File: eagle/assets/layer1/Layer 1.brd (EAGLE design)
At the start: 196 x 185.9 mm, 246 parts, among them M1C1 33nF, M1C2 680uF, M1C3 1.0uF, M1D1 RED, M1D2 BLUE, M1J1 XT30PB-F, M1Q1 AOD482, M1R1 1k, M1R10 1k, M1R11 10k, M1R12 4.7k, M1R2 1k, M1R3 3.3k, M1R4 3.3k, M1R5 1k, M1R6 1k, M1R7 1k, M1R8 10k, M1R9 10k, M2C1 33nF, M2C2 680uF, M2C3 1.0uF, M2D1 RED, M2D2 BLUE, M2J1 XT30PB-F, M2Q1 AOD482, M2R1 1k, M2R10 1k, M2R11 10k, M2R12 4.7k, M2R2 1k, M2R3 3.3k, M2R4 3.3k, M2R5 1k, M2R6 1k, M2R7 1k, M2R8 10k, M2R9 10k, M3C1 33nF, M3C2 680uF, M3C3 1.0uF, M3D1 RED, M3D2 BLUE, M3J1 XT30PB-F, M3Q1 AOD482, M3R1 1k, M3R10 1k, M3R11 10k, M3R12 4.7k, M3R2 1k, M3R3 3.3k, M3R4 3.3k, M3R5 1k, M3R6 1k, M3R7 1k, M3R8 10k, M3R9 10k, M4C1 33nF, M4C2 680uF, M4C3 1.0uF, M4D1 RED, M4D2 BLUE, M4J1 XT30PB-F, M4Q1 AOD482, M4R1 1k, M4R10 1k, M4R11 10k, M4R12 4.7k, M4R2 1k, M4R3 3.3k, M4R4 3.3k, M4R5 1k, M4R6 1k, M4R7 1k, M4R8 10k, M4R9 10k, Q37 AO3402, X2 SM06B-SRSS-TB, Y1 8MHz

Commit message: -
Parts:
- moved V_BATT_M4B 262.8 mm to (32.5, -82.0)
- moved GND_M2B 260.6 mm to (34.0, -59.5)
- moved GND_M4B 259.5 mm to (34.0, -62.0)
- moved V_BATT_M3B 251.3 mm to (32.5, -79.5)
- moved V_BATT_M2B 239.9 mm to (32.5, -77.0)
- moved V_BATT_M1B 228.7 mm to (32.5, -74.5)
- moved M3J1 47.8 mm to (-3.00, -39.5)
- moved M3D2 45.1 mm to (-7.00, -41.5), turned to 270 degrees
- moved M4J1 44.7 mm to (3.00, -39.5)
- moved M3R12 42.8 mm to (-8.80, -39.5), turned to 270 degrees
- moved M4D1 41.5 mm to (7.00, -41.5), turned to 90 degrees
- moved M3D1 40.8 mm to (-7.00, -37.5), turned to 270 degrees
- moved M4R12 37.0 mm to (8.80, -39.5), turned to 90 degrees
- moved M4D2 37.0 mm to (7.00, -37.5), turned to 90 degrees
- moved M2J1 33.3 mm to (3.00, 11.5)
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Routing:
- net N$83: track 0.00 -> 91.1 mm, vias 0 -> 1
- net N$84: track 0.00 -> 81.0 mm, vias 0 -> 1
- net N$53: track 0.00 -> 80.9 mm, vias 0 -> 1
- net N$85: track 0.00 -> 71.1 mm, vias 0 -> 1
- net N$54: track 0.00 -> 70.2 mm, vias 0 -> 1
- net N$98: track 0.00 -> 68.6 mm, vias 0 -> 3
- net N$68: track 0.00 -> 68.6 mm, vias 0 -> 1
- net N$86: track 0.00 -> 67.4 mm, vias 0 -> 1
- net N$103: track 0.00 -> 60.9 mm, vias 0 -> 1
- net N$97: track 0.00 -> 59.8 mm, vias 0 -> 3
- net N$55: track 0.00 -> 59.4 mm, vias 0 -> 1
- net N$67: track 0.00 -> 58.4 mm, vias 0 -> 1
- net N$96: track 0.00 -> 53.2 mm, vias 0 -> 3
- net N$102: track 0.00 -> 50.4 mm, vias 0 -> 1
- net N$87: track 0.00 -> 49.7 mm, vias 0 -> 1
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
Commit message: -
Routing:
- net N$103: track 60.9 -> 57.8 mm
- added copper zone on layer 1, net 3.3V

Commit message: 168 airwires left
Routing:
- net 3.3V: track 0.00 -> 176.3 mm, vias 0 -> 6
- net M_SWITCH: track 0.00 -> 108.9 mm, vias 0 -> 4
- net N$38: track 5.60 -> 68.2 mm, vias 0 -> 1
- net BR_DIR: track 0.00 -> 60.6 mm, vias 0 -> 4
- net NOT_FR_DIR: track 0.00 -> 56.6 mm, vias 0 -> 2
- net N$48: track 5.60 -> 61.8 mm
- net V_BATT: track 69.7 -> 124.5 mm
- net LS2: track 0.00 -> 54.3 mm, vias 0 -> 2
- net FR_DIR: track 0.00 -> 53.5 mm
- net LS3: track 0.00 -> 50.4 mm, vias 0 -> 2
- net NOT_BL_DIR: track 0.00 -> 47.1 mm, vias 0 -> 2
- net FL_DIR: track 0.00 -> 44.7 mm
- net N$18: track 5.49 -> 47.1 mm
- net N$28: track 5.49 -> 47.1 mm
- net 5V: track 0.00 -> 33.1 mm, vias 0 -> 1
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- added copper zone on layer 1, net 5V
- added copper zone on layer 1, net BL_OUTA
- added copper zone on layer 1, net BR_OUTA
- added copper zone on layer 1, net FL_OUTA
- added copper zone on layer 1, net FL_OUTB
- added copper zone on layer 1, net FR_OUTA
- added copper zone on layer 1, net FR_OUTB
- added copper zone on layer 1, net V_BATT

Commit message: 130 airwires left
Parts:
- moved C1 132.6 mm to (-27.6, 6.77), turned to 90 degrees
- moved C2 130.3 mm to (-26.1, 6.77), turned to 90 degrees
- moved C3 128.0 mm to (-24.6, 6.77), turned to 90 degrees
- moved 3C2 0.48 mm to (1.48, -6.99)
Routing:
- net 3.3V: track 176.3 -> 252.7 mm, vias 6 -> 9
- net GND: track 8.38 -> 73.4 mm, vias 3 -> 11
- net GND_M: track 23.9 -> 78.1 mm, vias 0 -> 6
- net V_BATT: track 124.5 -> 157.1 mm, vias 0 -> 2
- net BL_OUTB: track 35.6 -> 26.1 mm
- net NOT_FR_DIR: track 56.6 -> 57.7 mm
- net VCCA: track 463.1 -> 464.2 mm
- added copper zone on layer 16, net 3.3V
- added copper zone on layer 1, net BL_OUTB
- added copper zone on layer 1, net BR_OUTB

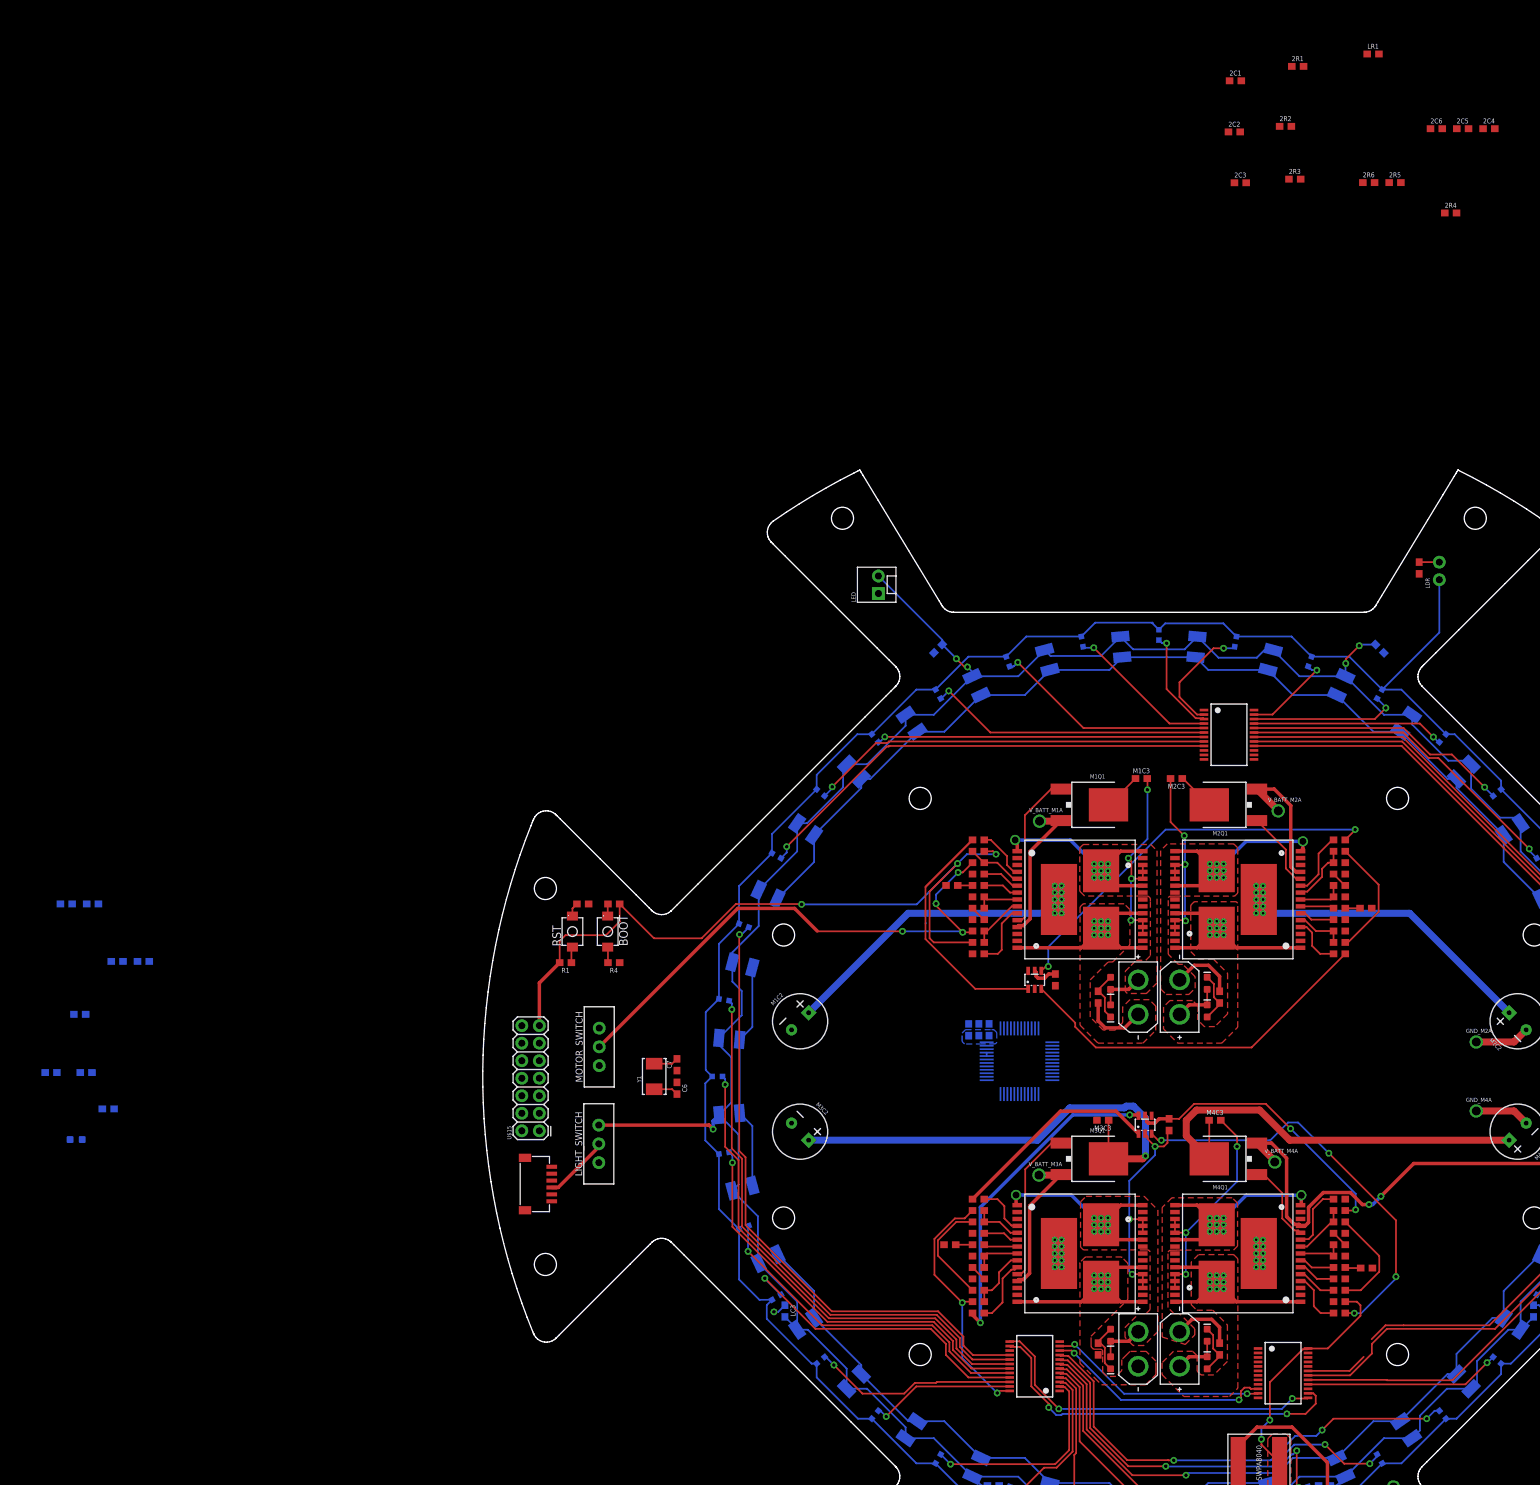
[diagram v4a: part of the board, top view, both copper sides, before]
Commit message: 121 airwires left mostly stm32
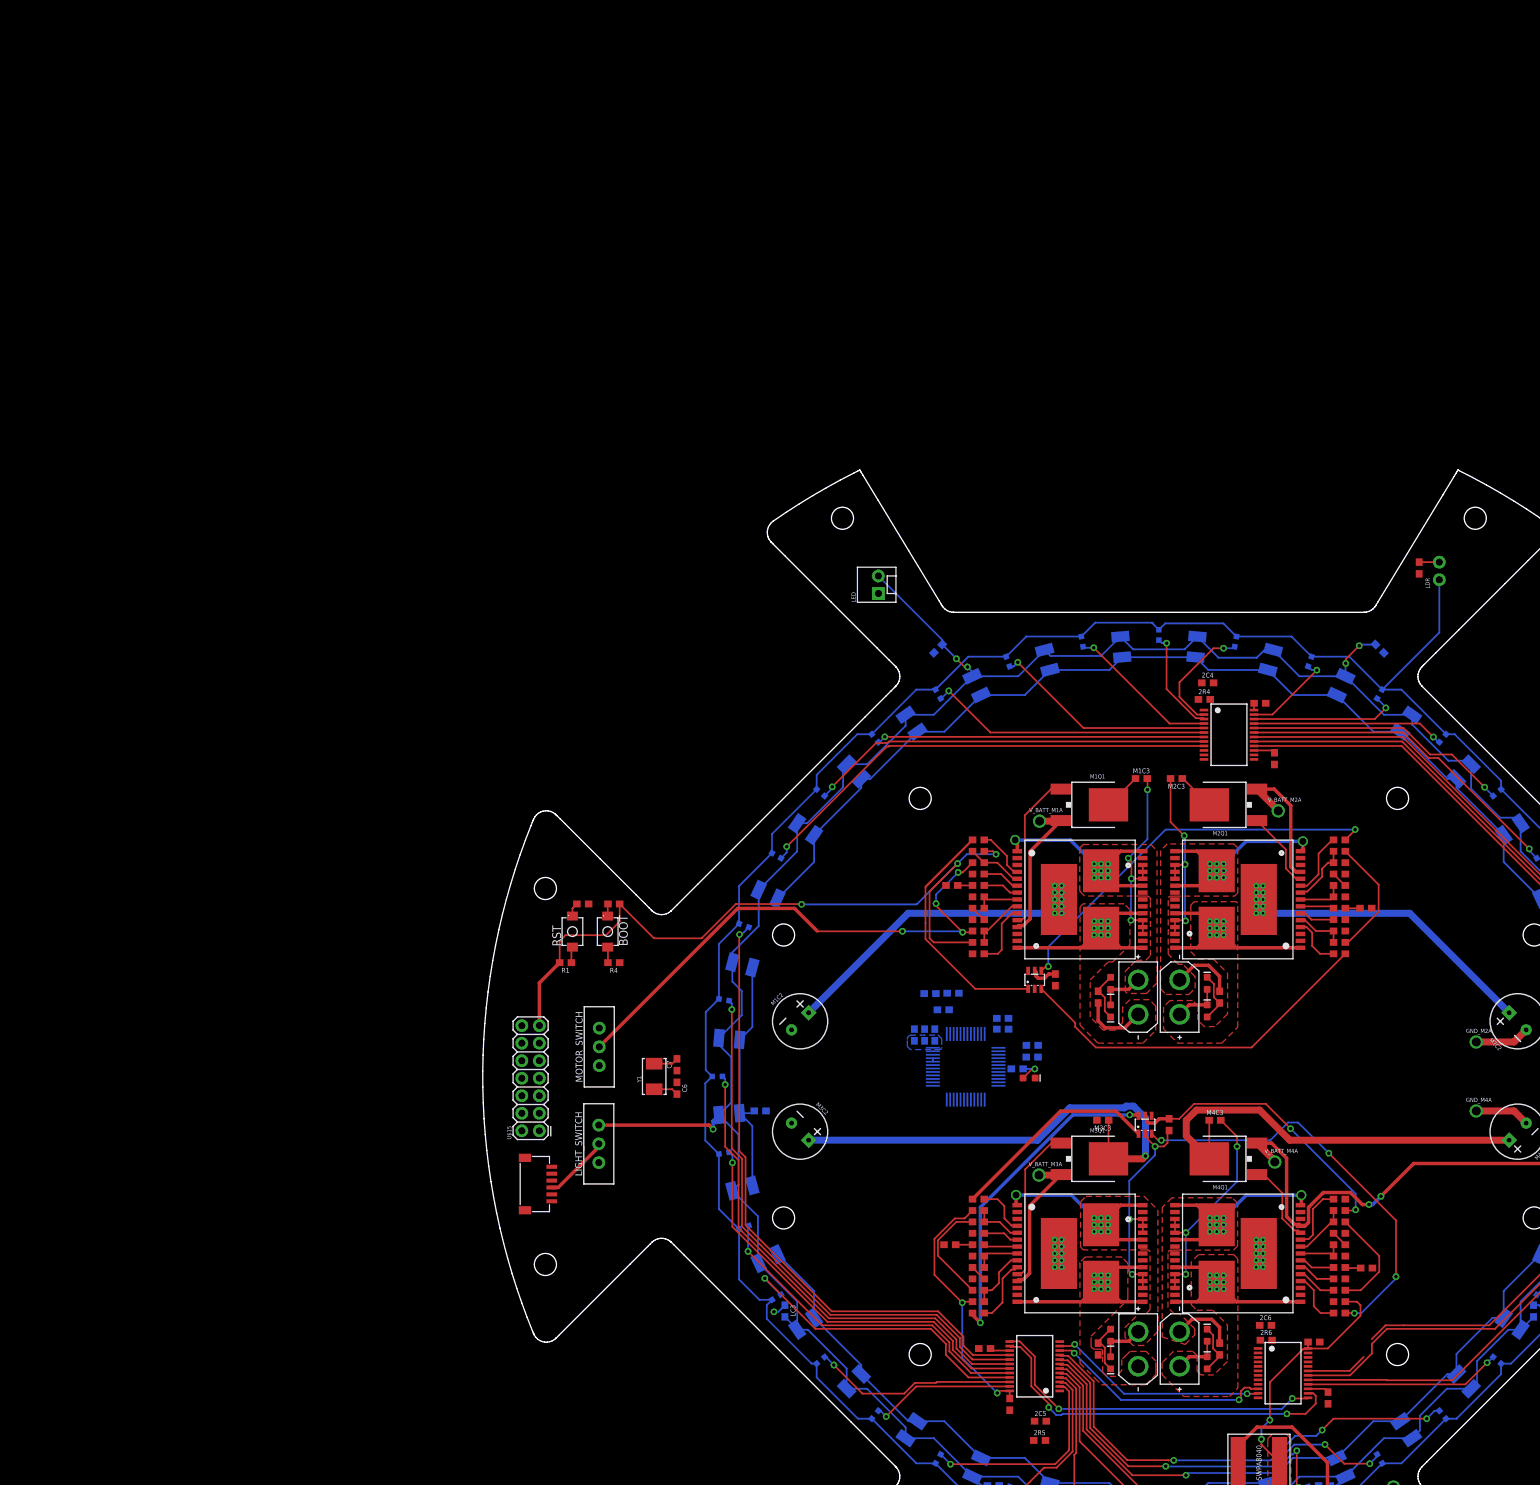
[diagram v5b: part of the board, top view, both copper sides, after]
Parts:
- moved 2C5 197.1 mm to (-17.2, -50.0)
- moved 2R5 189.5 mm to (-17.3, -52.8)
- moved 2C2 187.3 mm to (-21.6, -47.5), turned to 270 degrees
- moved 2R2 182.4 mm to (-25.3, -39.4)
- moved LR1 177.1 mm to (-57.8, -5.00), flipped to the bottom, turned to 180 degrees
- moved 2R3 176.7 mm to (24.5, -46.6), turned to 90 degrees
- moved 2C6 175.2 mm to (15.5, -36.1)
- moved 2R6 168.4 mm to (15.6, -38.2)
- moved 2C3 168.4 mm to (22.5, -38.5)
- moved D1 138.4 mm to (-18.8, -0.23), flipped to the top
- moved FB1 138.1 mm to (-22.6, 6.86)
- moved C8 133.8 mm to (-22.6, 8.42)
- moved R6 133.2 mm to (-18.4, 4.52), turned to 180 degrees
- moved R5 131.9 mm to (-20.5, 1.10)
- moved R7 129.6 mm to (-18.4, 2.81)
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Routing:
- net N$74: track 0.00 -> 3.98 mm, vias 0 -> 1
- net N$52: track 0.00 -> 3.11 mm
- net N$99: track 0.00 -> 3.09 mm
- net 3.3V: track 252.7 -> 255.7 mm
- net N$82: track 0.00 -> 2.90 mm
- net N$69: track 358.6 -> 360.9 mm

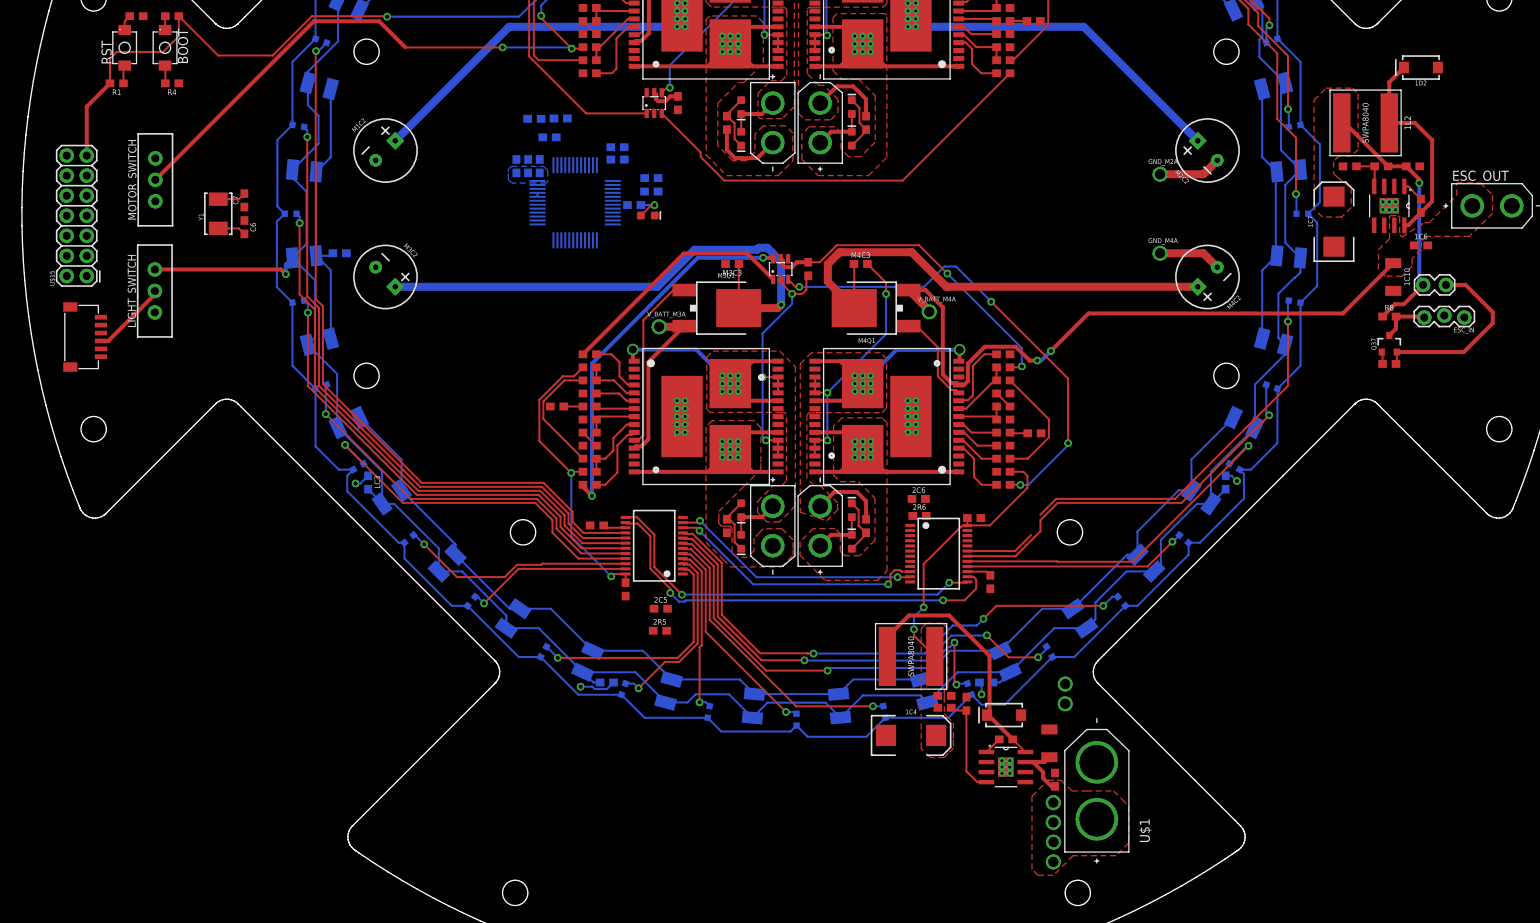
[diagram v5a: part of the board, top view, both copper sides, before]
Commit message: edited layer 1
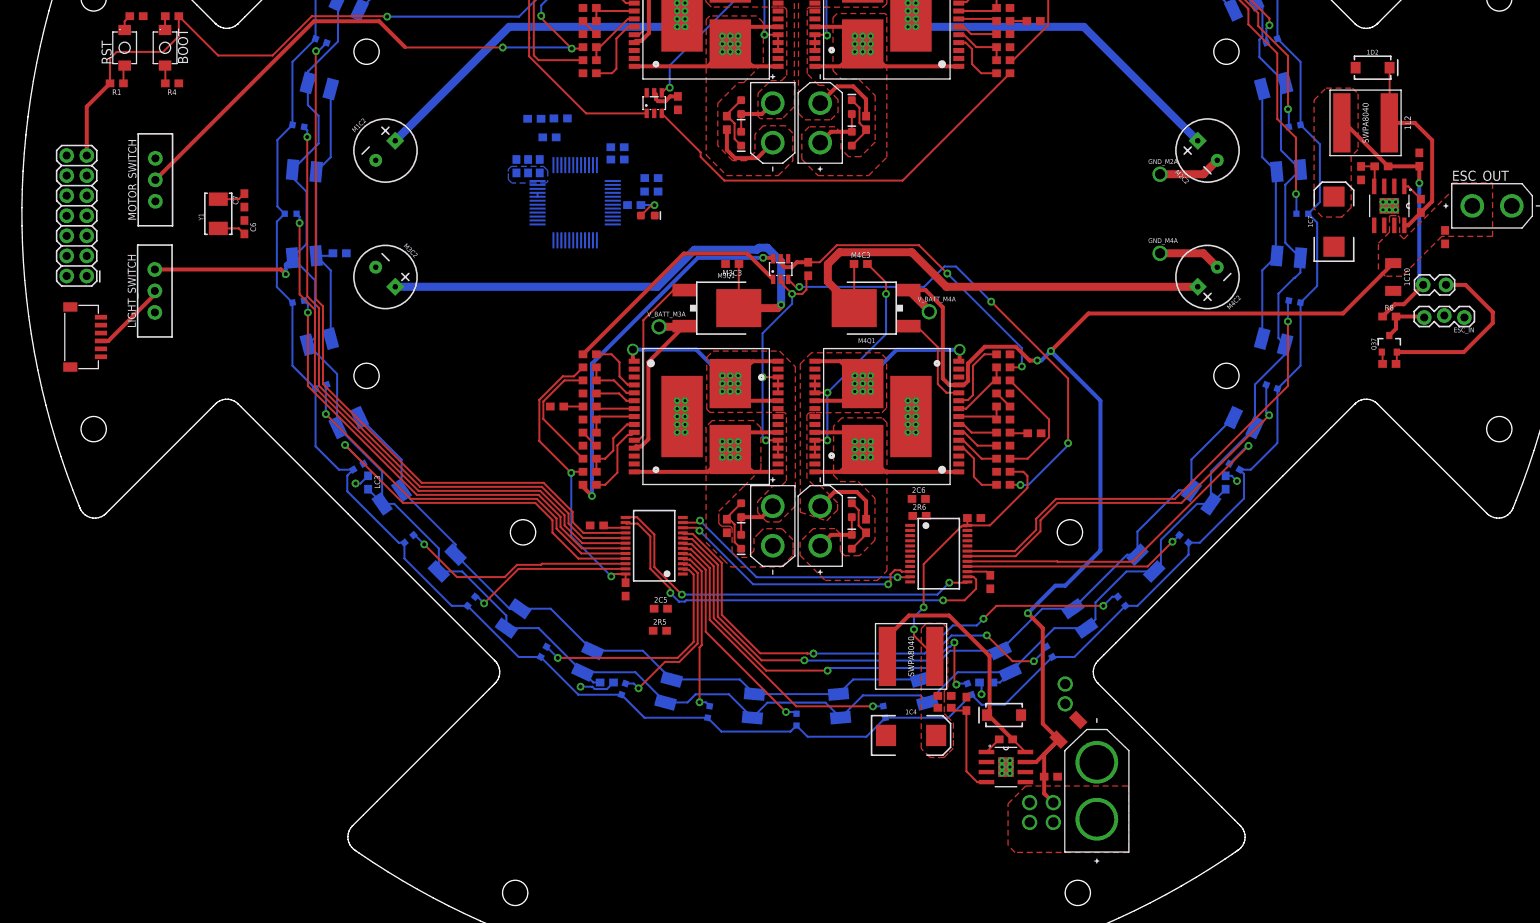
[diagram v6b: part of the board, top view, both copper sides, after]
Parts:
- moved 1D2 6.11 mm to (72.9, 18.5), turned to 0 degrees
- moved V_BATT_M3B 5.84 mm to (29.5, -74.5)
- moved V_BATT_M4B 5.83 mm to (29.5, -77.0)
- moved 1C6 3.23 mm to (82.1, -2.96), turned to 270 degrees
- moved 1C2 2.95 mm to (34.4, -65.3), turned to 45 degrees
- moved 1R4 1.67 mm to (71.4, 5.13), turned to 90 degrees
- moved 1C9 1.18 mm to (78.8, 6.86), turned to 90 degrees
- moved 1C1 0.64 mm to (32.2, -71.2), turned to 0 degrees
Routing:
- net V_BATT: track 157.1 -> 221.2 mm, vias 2 -> 3
- net N$103: track 57.8 -> 60.9 mm
- net 5V: track 33.1 -> 34.1 mm
- net N$3: track 26.6 -> 25.8 mm
- net N$49: track 12.0 -> 12.6 mm
- net N$5: track 4.86 -> 4.29 mm
